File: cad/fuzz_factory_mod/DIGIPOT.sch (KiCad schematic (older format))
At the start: 5 parts

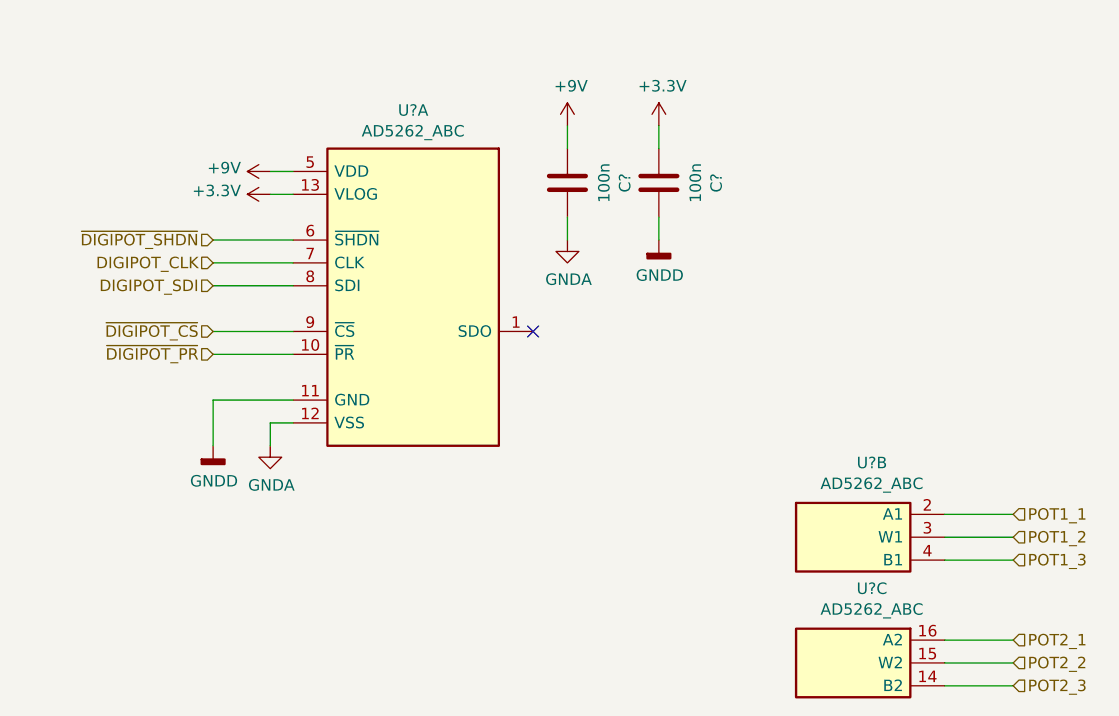
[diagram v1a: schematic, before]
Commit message: Continued schematic.
Modified fuuz_factory circuit : use of matched transistor pairs.
Added USB interface, through FT230X and direct to MCU.
Associated footprints, except for XTAL and trimmers.
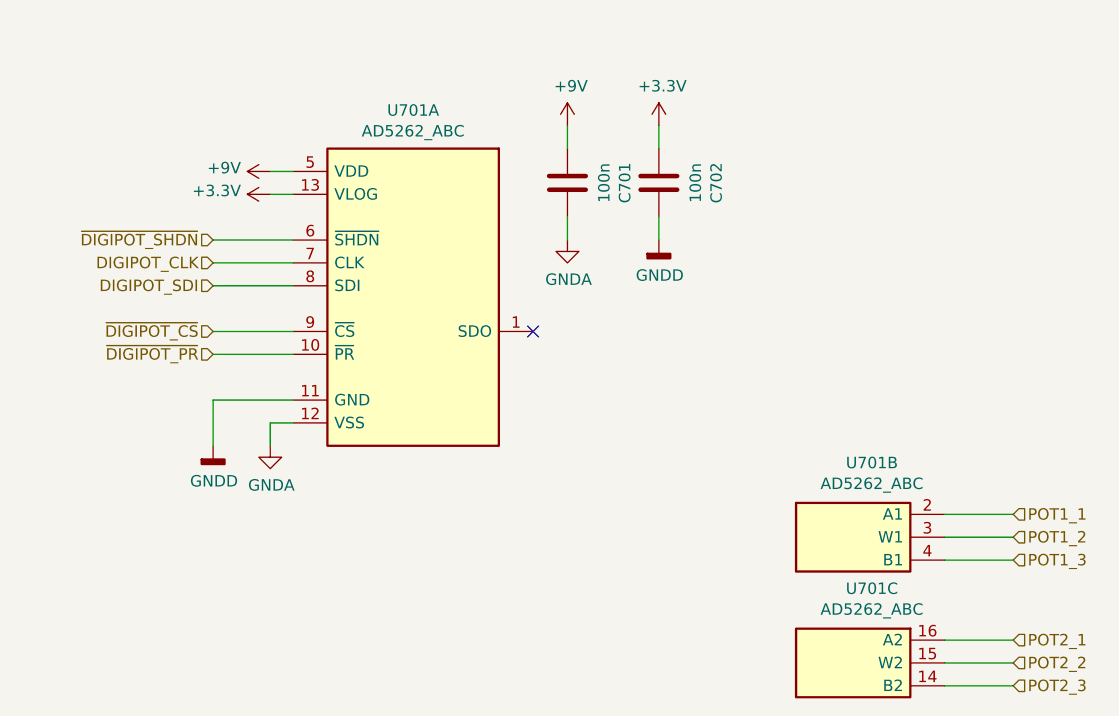
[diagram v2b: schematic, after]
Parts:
- C701, C702: renamed from C?; footprint (none) -> Capacitors_SMD:C_0603
- U701: renamed from U?; footprint (none) -> Housings_SSOP:TSSOP-16_4.4x5mm_Pitch0.65mm
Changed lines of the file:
@@
 $Descr A4 11693 8268
 encoding utf-8
-Sheet 5 19
+Sheet 7 22
 Title ""
 Date ""
@@
 P 5250 3800
 AR Path="/5DE4AD88/5E0E839D" Ref="#PWR?"  Part="1"
-AR Path="/5DE4AD88/5E0DD00B/5E0E839D" Ref="#PWR?"  Part="1"
+AR Path="/5DE4AD88/5E0DD00B/5E0E839D" Ref="#PWR0704"  Part="1"
 AR Path="/5DE4AD88/5E6E7BE0/5E6FDD0C/5E0E839D" Ref="#PWR?"  Part="1"
-F 0 "#PWR?" H 5250 3550 50  0001 C CNN
+F 0 "#PWR0704" H 5250 3550 50  0001 C CNN
 F 1 "GNDA" H 5255 3627 50  0000 C CNN
 F 2 "" H 5250 3800 50  0001 C CNN
@@
 P 5850 3200
 AR Path="/5DE4AD88/5E0E83A4" Ref="U?"  Part="1"
-AR Path="/5DE4AD88/5E0DD00B/5E0E83A4" Ref="U?"  Part="1"
+AR Path="/5DE4AD88/5E0DD00B/5E0E83A4" Ref="U701"  Part="1"
 AR Path="/5DE4AD88/5E6E7BE0/5E6FDD0C/5E0E83A4" Ref="U?"  Part="1"
-F 0 "U?" H 5875 4067 50  0000 C CNN
+F 0 "U701" H 5875 4067 50  0000 C CNN
 F 1 "AD5262_ABC" H 5875 3976 50  0000 C CNN
-F 2 "" H 5850 3200 50  0000 C CNN
+F 2 "Housings_SSOP:TSSOP-16_4.4x5mm_Pitch0.65mm" H 5850 3200 50  0001 C CNN
 F 3 "" H 5850 3200 50  0000 C CNN
 	1    5850 3200
@@
 P 5000 3800
 AR Path="/5DE4AD88/5E0E83AB" Ref="#PWR?"  Part="1"
-AR Path="/5DE4AD88/5E0DD00B/5E0E83AB" Ref="#PWR?"  Part="1"
+AR Path="/5DE4AD88/5E0DD00B/5E0E83AB" Ref="#PWR0701"  Part="1"
 AR Path="/5DE4AD88/5E6E7BE0/5E6FDD0C/5E0E83AB" Ref="#PWR?"  Part="1"
-F 0 "#PWR?" H 5000 3550 50  0001 C CNN
+F 0 "#PWR0701" H 5000 3550 50  0001 C CNN
 F 1 "GNDD" H 5004 3645 50  0000 C CNN
 F 2 "" H 5000 3800 50  0001 C CNN
@@
 P 5250 2700
 AR Path="/5DE4AD88/5E0E83B4" Ref="#PWR?"  Part="1"
-AR Path="/5DE4AD88/5E0DD00B/5E0E83B4" Ref="#PWR?"  Part="1"
+AR Path="/5DE4AD88/5E0DD00B/5E0E83B4" Ref="#PWR0703"  Part="1"
 AR Path="/5DE4AD88/5E6E7BE0/5E6FDD0C/5E0E83B4" Ref="#PWR?"  Part="1"
-F 0 "#PWR?" H 5250 2550 50  0001 C CNN
+F 0 "#PWR0703" H 5250 2550 50  0001 C CNN
 F 1 "+3.3V" V 5265 2828 50  0000 L CNN
 F 2 "" H 5250 2700 50  0001 C CNN
@@
 P 5250 2600
 AR Path="/5DE4AD88/5E0E83BA" Ref="#PWR?"  Part="1"
-AR Path="/5DE4AD88/5E0DD00B/5E0E83BA" Ref="#PWR?"  Part="1"
+AR Path="/5DE4AD88/5E0DD00B/5E0E83BA" Ref="#PWR0702"  Part="1"
 AR Path="/5DE4AD88/5E6E7BE0/5E6FDD0C/5E0E83BA" Ref="#PWR?"  Part="1"
-F 0 "#PWR?" H 5250 2450 50  0001 C CNN
+F 0 "#PWR0702" H 5250 2450 50  0001 C CNN
 F 1 "+9V" V 5265 2728 50  0000 L CNN
 F 2 "" H 5250 2600 50  0001 C CNN
@@
 P 6550 2650
 AR Path="/5DE4AD88/5E0E83C2" Ref="C?"  Part="1"
-AR Path="/5DE4AD88/5E0DD00B/5E0E83C2" Ref="C?"  Part="1"
+AR Path="/5DE4AD88/5E0DD00B/5E0E83C2" Ref="C701"  Part="1"
 AR Path="/5DE4AD88/5E6E7BE0/5E6FDD0C/5E0E83C2" Ref="C?"  Part="1"
-F 0 "C?" V 6298 2650 50  0000 C CNN
+F 0 "C701" V 6298 2650 50  0000 C CNN
 F 1 "100n" V 6389 2650 50  0000 C CNN
-F 2 "" H 6588 2500 50  0001 C CNN
+F 2 "Capacitors_SMD:C_0603" H 6588 2500 50  0001 C CNN
 F 3 "~" H 6550 2650 50  0001 C CNN
 	1    6550 2650
@@
 P 6550 2400
 AR Path="/5DE4AD88/5E0E83C8" Ref="#PWR?"  Part="1"
-AR Path="/5DE4AD88/5E0DD00B/5E0E83C8" Ref="#PWR?"  Part="1"
+AR Path="/5DE4AD88/5E0DD00B/5E0E83C8" Ref="#PWR0705"  Part="1"
 AR Path="/5DE4AD88/5E6E7BE0/5E6FDD0C/5E0E83C8" Ref="#PWR?"  Part="1"
-F 0 "#PWR?" H 6550 2250 50  0001 C CNN
+F 0 "#PWR0705" H 6550 2250 50  0001 C CNN
 F 1 "+9V" H 6565 2573 50  0000 C CNN
 F 2 "" H 6550 2400 50  0001 C CNN
@@
 P 6550 2900
 AR Path="/5DE4AD88/5E0E83CE" Ref="#PWR?"  Part="1"
-AR Path="/5DE4AD88/5E0DD00B/5E0E83CE" Ref="#PWR?"  Part="1"
+AR Path="/5DE4AD88/5E0DD00B/5E0E83CE" Ref="#PWR0706"  Part="1"
 AR Path="/5DE4AD88/5E6E7BE0/5E6FDD0C/5E0E83CE" Ref="#PWR?"  Part="1"
-F 0 "#PWR?" H 6550 2650 50  0001 C CNN
+F 0 "#PWR0706" H 6550 2650 50  0001 C CNN
 F 1 "GNDA" H 6555 2727 50  0000 C CNN
 F 2 "" H 6550 2900 50  0001 C CNN
@@
 P 6950 2400
 AR Path="/5DE4AD88/5E0E83D6" Ref="#PWR?"  Part="1"
-AR Path="/5DE4AD88/5E0DD00B/5E0E83D6" Ref="#PWR?"  Part="1"
+AR Path="/5DE4AD88/5E0DD00B/5E0E83D6" Ref="#PWR0707"  Part="1"
 AR Path="/5DE4AD88/5E6E7BE0/5E6FDD0C/5E0E83D6" Ref="#PWR?"  Part="1"
-F 0 "#PWR?" H 6950 2250 50  0001 C CNN
+F 0 "#PWR0707" H 6950 2250 50  0001 C CNN
 F 1 "+3.3V" H 6965 2573 50  0000 C CNN
 F 2 "" H 6950 2400 50  0001 C CNN
@@
 P 6950 2650
 AR Path="/5DE4AD88/5E0E83DC" Ref="C?"  Part="1"
-AR Path="/5DE4AD88/5E0DD00B/5E0E83DC" Ref="C?"  Part="1"
+AR Path="/5DE4AD88/5E0DD00B/5E0E83DC" Ref="C702"  Part="1"
 AR Path="/5DE4AD88/5E6E7BE0/5E6FDD0C/5E0E83DC" Ref="C?"  Part="1"
-F 0 "C?" V 6698 2650 50  0000 C CNN
+F 0 "C702" V 6698 2650 50  0000 C CNN
 F 1 "100n" V 6789 2650 50  0000 C CNN
-F 2 "" H 6988 2500 50  0001 C CNN
+F 2 "Capacitors_SMD:C_0603" H 6988 2500 50  0001 C CNN
 F 3 "~" H 6950 2650 50  0001 C CNN
 	1    6950 2650
@@
 P 6950 2900
 AR Path="/5DE4AD88/5E0E83E2" Ref="#PWR?"  Part="1"
-AR Path="/5DE4AD88/5E0DD00B/5E0E83E2" Ref="#PWR?"  Part="1"
+AR Path="/5DE4AD88/5E0DD00B/5E0E83E2" Ref="#PWR0708"  Part="1"
 AR Path="/5DE4AD88/5E6E7BE0/5E6FDD0C/5E0E83E2" Ref="#PWR?"  Part="1"
-F 0 "#PWR?" H 6950 2650 50  0001 C CNN
+F 0 "#PWR0708" H 6950 2650 50  0001 C CNN
 F 1 "GNDD" H 6954 2745 50  0000 C CNN
 F 2 "" H 6950 2900 50  0001 C CNN
@@
 ~DIGIPOT_PR
 $Comp
-L flax_lib:AD5262_ABC U?
+L flax_lib:AD5262_ABC U701
 U 2 1 5E0EEEE6
 P 7800 4200
-AR Path="/5DE4AD88/5E0DD00B/5E0EEEE6" Ref="U?"  Part="2"
+AR Path="/5DE4AD88/5E0DD00B/5E0EEEE6" Ref="U701"  Part="2"
 AR Path="/5DE4AD88/5E6E7BE0/5E6FDD0C/5E0EEEE6" Ref="U?"  Part="2"
-F 0 "U?" H 7882 4525 50  0000 C CNN
+F 0 "U701" H 7882 4525 50  0000 C CNN
 F 1 "AD5262_ABC" H 7882 4434 50  0000 C CNN
-F 2 "" H 7800 4200 50  0000 C CNN
+F 2 "Housings_SSOP:TSSOP-16_4.4x5mm_Pitch0.65mm" H 7800 4200 50  0001 C CNN
 F 3 "" H 7800 4200 50  0000 C CNN
 	2    7800 4200
@@
 $EndComp
 $Comp
-L flax_lib:AD5262_ABC U?
+L flax_lib:AD5262_ABC U701
 U 3 1 5E0EEEEC
 P 7800 4750
-AR Path="/5DE4AD88/5E0DD00B/5E0EEEEC" Ref="U?"  Part="3"
+AR Path="/5DE4AD88/5E0DD00B/5E0EEEEC" Ref="U701"  Part="3"
 AR Path="/5DE4AD88/5E6E7BE0/5E6FDD0C/5E0EEEEC" Ref="U?"  Part="3"
-F 0 "U?" H 7882 5075 50  0000 C CNN
+F 0 "U701" H 7882 5075 50  0000 C CNN
 F 1 "AD5262_ABC" H 7882 4984 50  0000 C CNN
-F 2 "" H 7800 4750 50  0000 C CNN
+F 2 "Housings_SSOP:TSSOP-16_4.4x5mm_Pitch0.65mm" H 7800 4750 50  0001 C CNN
 F 3 "" H 7800 4750 50  0000 C CNN
 	3    7800 4750

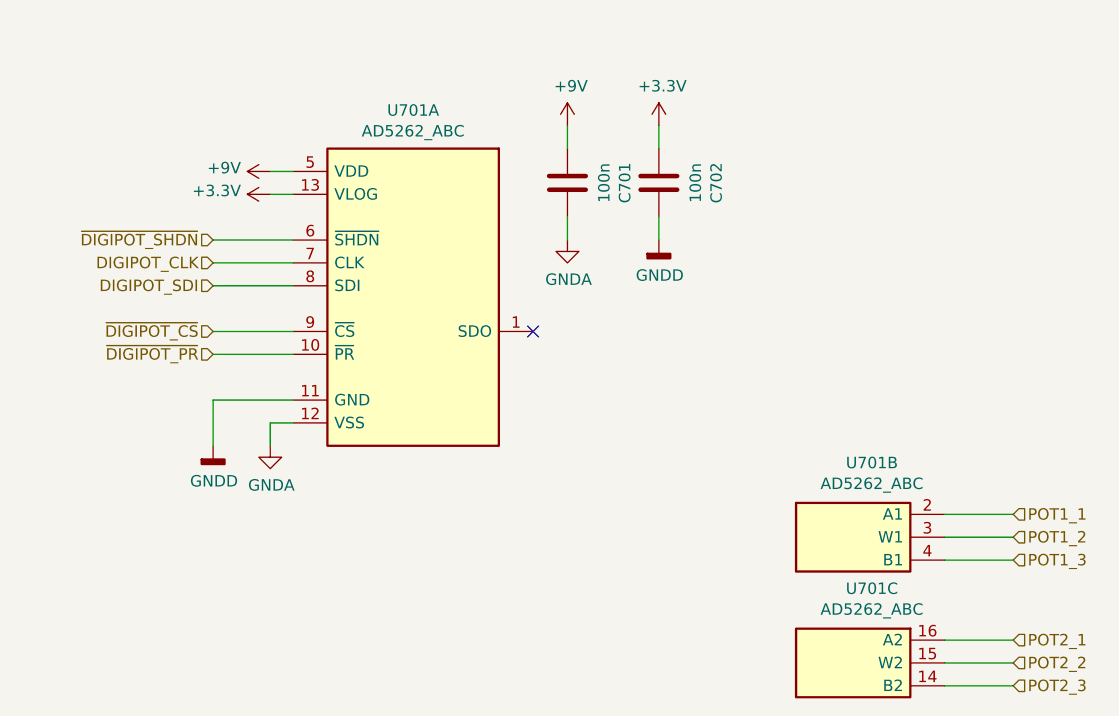
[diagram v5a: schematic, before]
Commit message: Changes architecture.
Corrections on schematic.
Continued Layout placement.
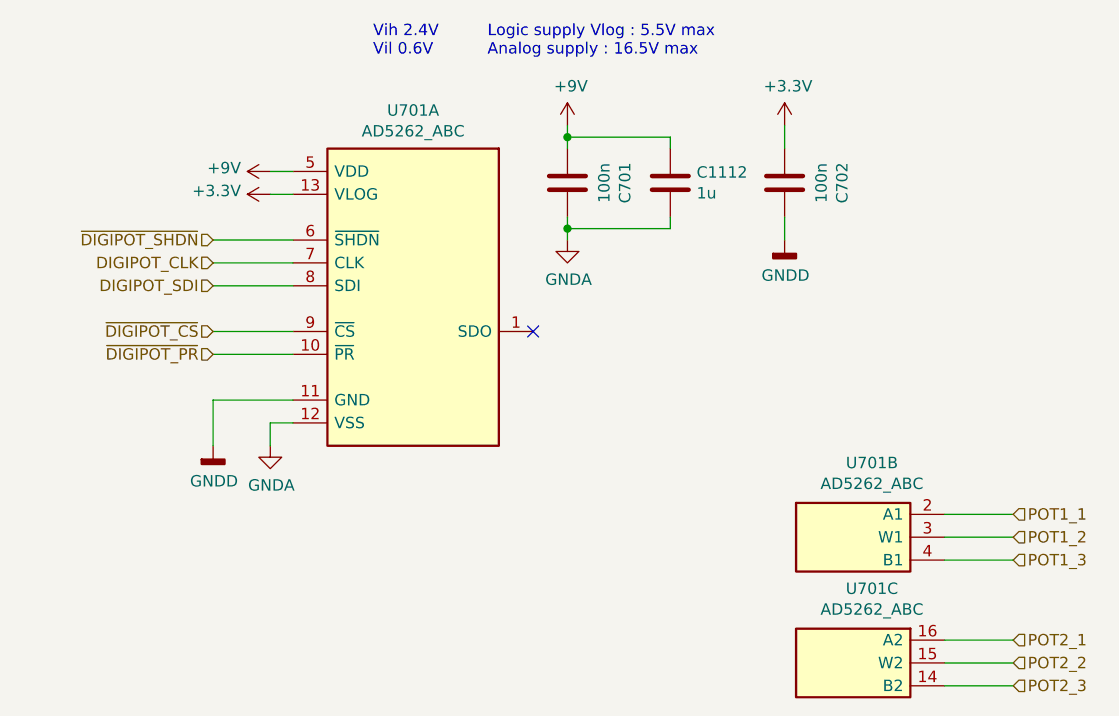
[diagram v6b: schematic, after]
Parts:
- added C1112: 1u, Capacitors_SMD:C_0805, symbol Device:C
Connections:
- net +9V: now also C1112.1
- net GNDA: now also C1112.2
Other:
- note added: "Logic supply Vlog : 5.5V max\nAnalog supply : 16.5V max"
- note added: "Vih 2.4V\nVil 0.6V"
- moved on the sheet: C702
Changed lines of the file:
@@
 $Descr A4 11693 8268
 encoding utf-8
-Sheet 15 30
+Sheet 11 22
 Title ""
 Date ""
@@
 $EndComp
 Wire Wire Line
-	6550 2800 6550 2900
-Wire Wire Line
-	6550 2500 6550 2400
+	6550 2800 6550 2850
+Wire Wire Line
+	6550 2500 6550 2450
 $Comp
 L power:+3.3V #PWR?
 U 1 1 5E0E83D6
-P 6950 2400
+P 7500 2400
 AR Path="/5DE4AD88/5E0E83D6" Ref="#PWR?"  Part="1"
 AR Path="/5DE4AD88/5E0DD00B/5E0E83D6" Ref="#PWR0707"  Part="1"
 AR Path="/5DE4AD88/5E6E7BE0/5E6FDD0C/5E0E83D6" Ref="#PWR?"  Part="1"
-F 0 "#PWR0707" H 6950 2250 50  0001 C CNN
-F 1 "+3.3V" H 6965 2573 50  0000 C CNN
-F 2 "" H 6950 2400 50  0001 C CNN
-F 3 "" H 6950 2400 50  0001 C CNN
-	1    6950 2400
+F 0 "#PWR0707" H 7500 2250 50  0001 C CNN
+F 1 "+3.3V" H 7515 2573 50  0000 C CNN
+F 2 "" H 7500 2400 50  0001 C CNN
+F 3 "" H 7500 2400 50  0001 C CNN
+	1    7500 2400
 	1    0    0    -1
 $EndComp
@@
 L Device:C C?
 U 1 1 5E0E83DC
-P 6950 2650
+P 7500 2650
 AR Path="/5DE4AD88/5E0E83DC" Ref="C?"  Part="1"
 AR Path="/5DE4AD88/5E0DD00B/5E0E83DC" Ref="C702"  Part="1"
 AR Path="/5DE4AD88/5E6E7BE0/5E6FDD0C/5E0E83DC" Ref="C?"  Part="1"
-F 0 "C702" V 6698 2650 50  0000 C CNN
-F 1 "100n" V 6789 2650 50  0000 C CNN
-F 2 "Capacitors_SMD:C_0603" H 6988 2500 50  0001 C CNN
-F 3 "~" H 6950 2650 50  0001 C CNN
-	1    6950 2650
+F 0 "C702" V 7248 2650 50  0000 C CNN
+F 1 "100n" V 7339 2650 50  0000 C CNN
+F 2 "Capacitors_SMD:C_0603" H 7538 2500 50  0001 C CNN
+F 3 "~" H 7500 2650 50  0001 C CNN
+	1    7500 2650
 	-1   0    0    1
 $EndComp
@@
 L power:GNDD #PWR?
 U 1 1 5E0E83E2
-P 6950 2900
+P 7500 2900
 AR Path="/5DE4AD88/5E0E83E2" Ref="#PWR?"  Part="1"
 AR Path="/5DE4AD88/5E0DD00B/5E0E83E2" Ref="#PWR0708"  Part="1"
 AR Path="/5DE4AD88/5E6E7BE0/5E6FDD0C/5E0E83E2" Ref="#PWR?"  Part="1"
-F 0 "#PWR0708" H 6950 2650 50  0001 C CNN
-F 1 "GNDD" H 6954 2745 50  0000 C CNN
-F 2 "" H 6950 2900 50  0001 C CNN
-F 3 "" H 6950 2900 50  0001 C CNN
-	1    6950 2900
-	1    0    0    -1
-$EndComp
-Wire Wire Line
-	6950 2800 6950 2900
-Wire Wire Line
-	6950 2400 6950 2500
+F 0 "#PWR0708" H 7500 2650 50  0001 C CNN
+F 1 "GNDD" H 7504 2745 50  0000 C CNN
+F 2 "" H 7500 2900 50  0001 C CNN
+F 3 "" H 7500 2900 50  0001 C CNN
+	1    7500 2900
+	1    0    0    -1
+$EndComp
+Wire Wire Line
+	7500 2800 7500 2900
+Wire Wire Line
+	7500 2400 7500 2500
 Text HLabel 5000 2900 0    50   Input ~ 0
 ~DIGIPOT_SHDN
@@
 Wire Wire Line
 	8500 4850 8200 4850
+Text Notes 5700 2100 0    50   ~ 0
+Vih 2.4V\nVil 0.6V
+Text Notes 6200 2100 0    50   ~ 0
+Logic supply Vlog : 5.5V max\nAnalog supply : 16.5V max
+$Comp
+L Device:C C?
+U 1 1 5F1F336B
+P 7000 2650
+AR Path="/5DE4AD26/5F1F336B" Ref="C?"  Part="1"
+AR Path="/5DE4AD88/5E0DD00B/5F1F336B" Ref="C1112"  Part="1"
+F 0 "C1112" H 7115 2696 50  0000 L CNN
+F 1 "1u" H 7115 2605 50  0000 L CNN
+F 2 "Capacitors_SMD:C_0805" H 7038 2500 50  0001 C CNN
+F 3 "~" H 7000 2650 50  0001 C CNN
+	1    7000 2650
+	1    0    0    -1
+$EndComp
+Wire Wire Line
+	7000 2500 7000 2450
+Wire Wire Line
+	7000 2450 6550 2450
+Connection ~ 6550 2450
+Wire Wire Line
+	6550 2450 6550 2400
+Wire Wire Line
+	7000 2800 7000 2850
+Wire Wire Line
+	7000 2850 6550 2850
+Connection ~ 6550 2850
+Wire Wire Line
+	6550 2850 6550 2900
 $EndSCHEMATC
